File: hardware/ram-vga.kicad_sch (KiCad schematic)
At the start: 63 parts, among them J11 GPCO, J6 DB15_Female_HighDensity, J7 Conn_01x12_Male, U10 74HC245, U11 74HC245, U12 74HC109, U14 74HC04, U16 62256, U17 74HC00, U18 w27C512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

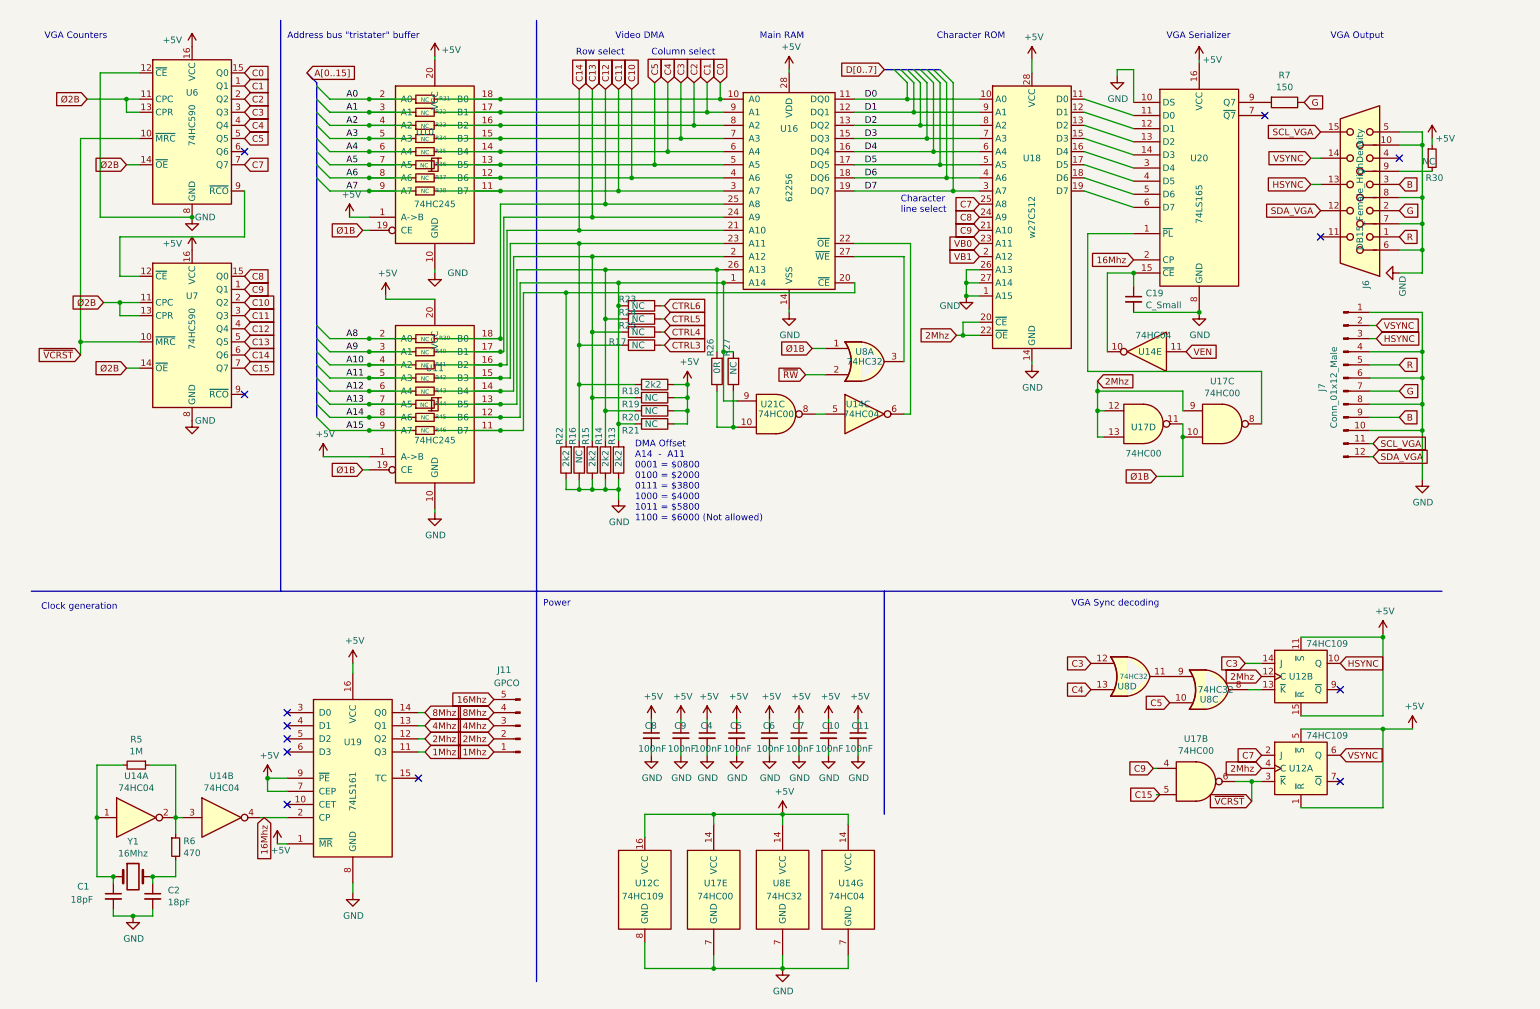
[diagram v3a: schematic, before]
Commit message: Silkscreen indicators, updated BOM and gerbers and stuff
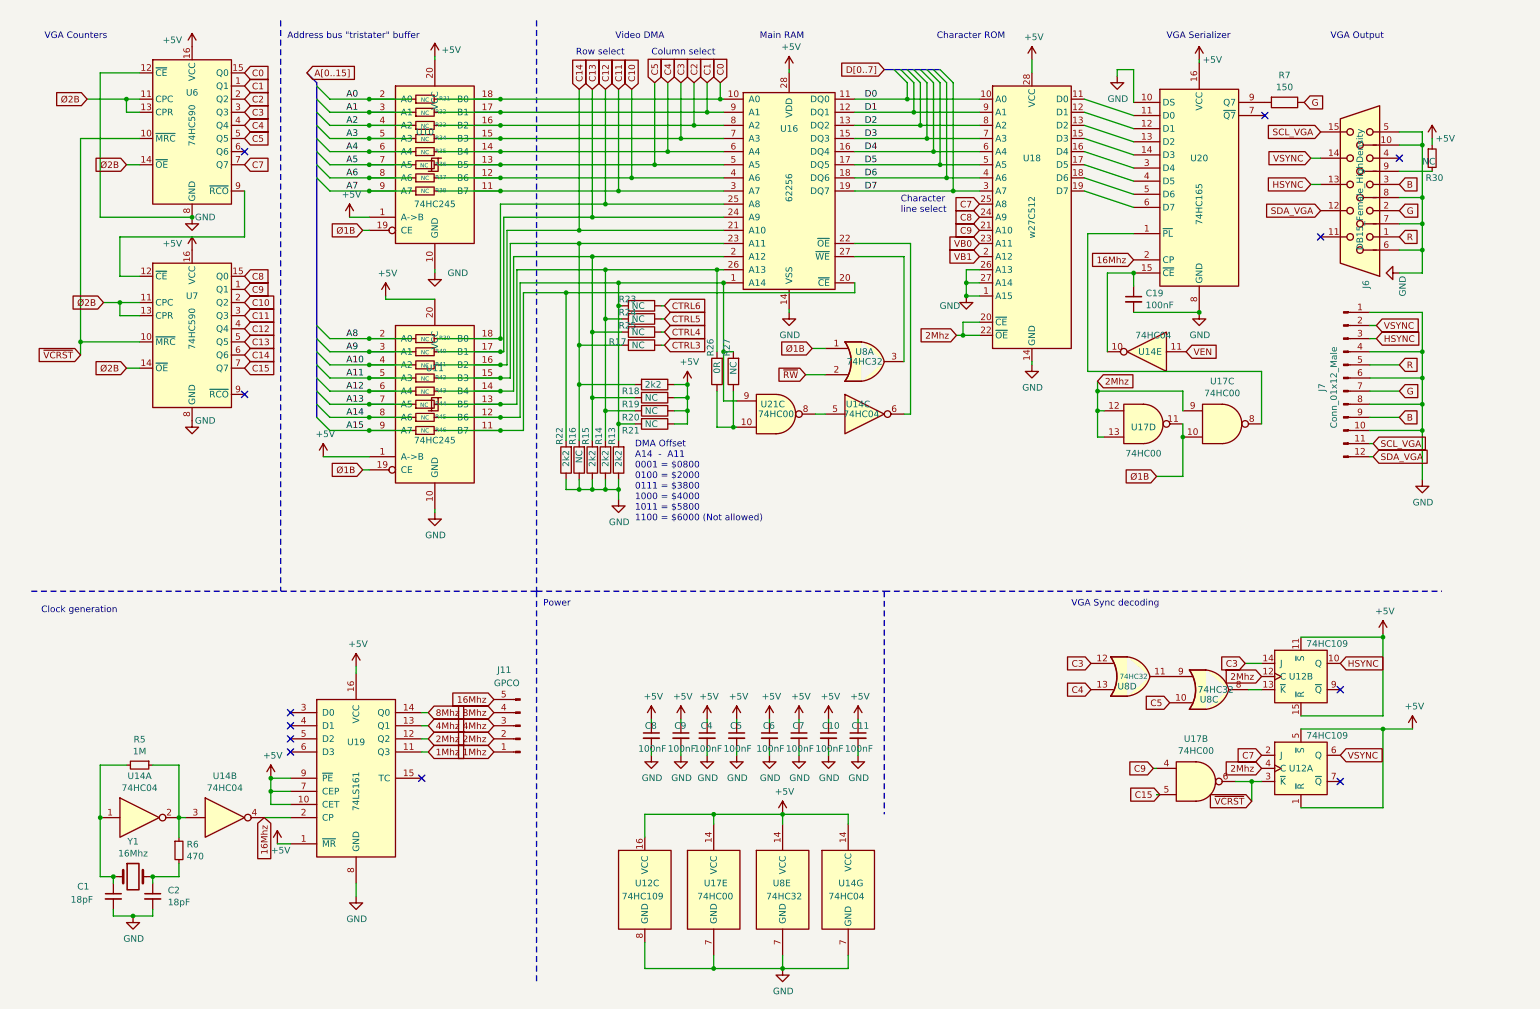
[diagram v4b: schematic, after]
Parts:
- C19: value C_Small -> 100nF
- U20: value 74LS165 -> 74HC165
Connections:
- net +5V: now also U19.10 (CET)
- no-connect marks 13 -> 12
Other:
- moved on the sheet: R5, R6, U14A, U14B, U19

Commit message: Revision 2 published
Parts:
- added Y2: 16Mhz, Crystal:Crystal_SMD_3225-4Pin_3.2x2.5mm, symbol Device:Crystal_GND24
- C1, C2: value 18pF -> 14pF; LCSC (none) -> C519919
- C10, C11, C19, C4, C5, C6, C7, C8, C9: LCSC (none) -> C14663
- J6: footprint Connector_Dsub:DSUB-15-HD_Female_Horizontal_P2.29x2.54mm_EdgePinOffset9.40mm-Mountingholes -> Connector_Dsub:DSUB-15-HD_Female_Horizontal_P2.29x1.98mm_EdgePinOffset8.35mm_Housed_MountingHolesOffset10.89mm; LCSC (none) -> C138387
- J7, R16, R19, R20, R21, Y1: now not fitted
- R13, R14, R15, R18: LCSC (none) -> C114561; now not fitted
- R17, R23, R24, R25: value NC -> 2k2; LCSC (none) -> C114561
- R22: LCSC (none) -> C114561
- R26: footprint Jumper:SolderJumper-2_P1.3mm_Open_RoundedPad1.0x1.5mm -> Jumper:SolderJumper-2_P1.3mm_Bridged_RoundedPad1.0x1.5mm; symbol Device:R -> Jumper:SolderJumper_2_Bridged; now left out of the parts list
- R27: symbol Device:R -> Jumper:SolderJumper_2_Open; now left out of the parts list
- R5: LCSC (none) -> C17514
- R6: LCSC (none) -> C17710
- R7: LCSC (none) -> C17471
- U10, U11: LCSC (none) -> C72118
- U12, U19, U20, U6, U7: LCSC (none) -> C72115
- U14, U17, U21, U8: LCSC (none) -> C2325
- U16, U18: LCSC (none) -> C72121
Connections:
- net GND: now also Y2.2, Y2.4
- net at C1.1, R5.2, U14.1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: now also Y2.1
- net at C2.1, R6.2, Y1.2: now also Y2.3
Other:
- note added: "R26 R27 $4000-5fff Closed Cut Range is RAM Cut Closed Range is unallocated"
- moved on the sheet: R22, R5, U14A
